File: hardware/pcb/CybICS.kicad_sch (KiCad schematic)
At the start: 75 parts, among them J1 Raspberry_Pi_2_3, J2 Conn_01x03_Pin, J3 Conn_01x05_Pin, SW1 SW_Push, SW2 SW_Push, SW3 SW_Push, U1 STM32G070RBTx

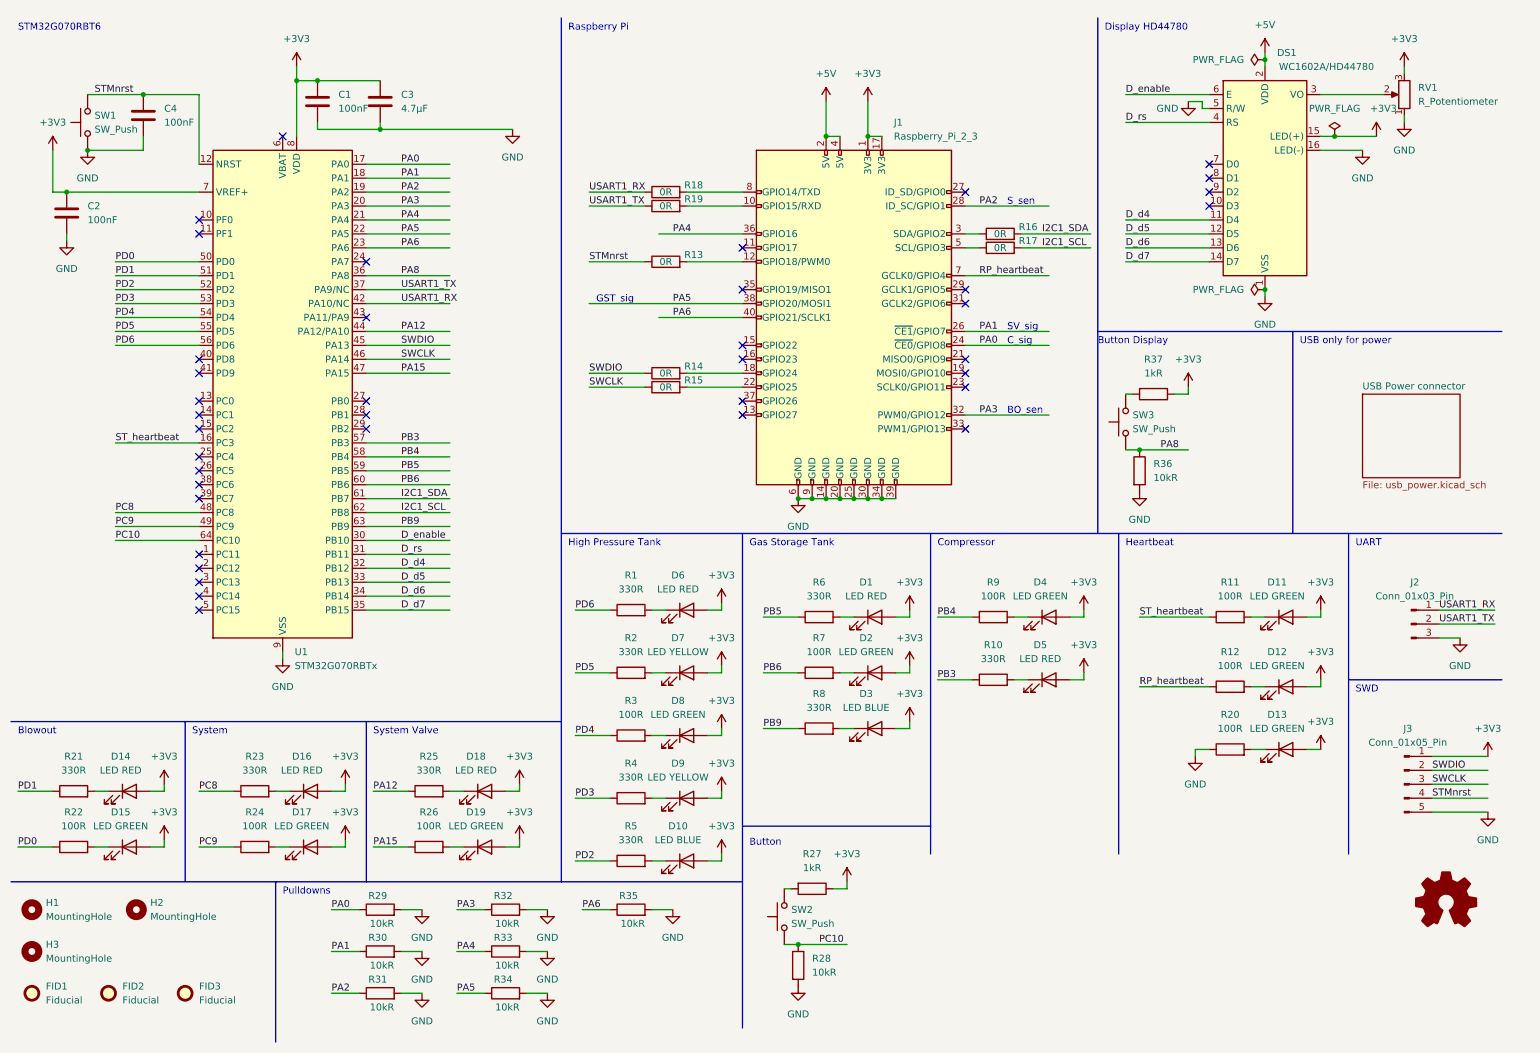
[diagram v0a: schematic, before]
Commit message: feat(hardware)!: hardware v1.1 upgrade, KiCad 10 and JLCPCB fixes (#240)
* fix(hardware): exclude fiducials from the JLCPCB position files

FID1-FID3 carried exclude_from_bom but not exclude_from_pos_files,
unlike the mounting holes and the OSHW logo, which set both. The
fiducials therefore reached the CPL while being absent from the BOM,
and JLCPCB rejected the assembly quote with "FID1,FID2,FID3
designators don't exist in the BOM file" (reported in #238). Fiducials
are alignment marks rather than parts, so the dialog was harmless, but
every person ordering this board had to decide that for themselves.

Verified with kicad-cli 8.0.9: pcb export pos --smd-only drops from 69
to 66 rows against the previous board, the three removed designators
are exactly FID1, FID2 and FID3, and ERC and DRC still report 0
violations and 0 unconnected items. Claude has no access to the
hardware, so the JLCPCB upload itself is unverified.

Refs #238

Co-Authored-By: Claude Opus 5 (1M context) <noreply@anthropic.com>
Claude-Session: https://claude.ai/code/session_011zbigHZaGiZii3etPu8DwT

* fix(hardware): correct the LED series resistors and the yellow LED part

R1/R2/R4/R6/R10/R21/R23/R25 are drawn as 330R but carried C52548, which
is 0805W8F330LT5E -- 330 mΩ, not 330 Ω. The L in that part code is
Uniroyal's milliohm marker, and both LCSC and JLCPCB's parts database
index it at 0.33 Ω. The six red, two yellow and two blue indicators
were therefore assembled with no effective current limiting: each one
settles at roughly its full rated current against the GPIO's own
impedance, and ten such pins take the STM32G070 past its 100 mA total
I/O budget. Corrected to C17630 (0805W8F3300T5E, 330 Ω), which is also
a basic-library part.

That correction alone would have regressed two colours, because the
0.33 Ω part was the only reason they lit at all:

  - D7/D9 are drawn as LED YELLOW but carried C434441, SZYY1206W -- a
    *white* LED with a yellow lens and Vf 3.1 V. Across a real 330 Ω
    fro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
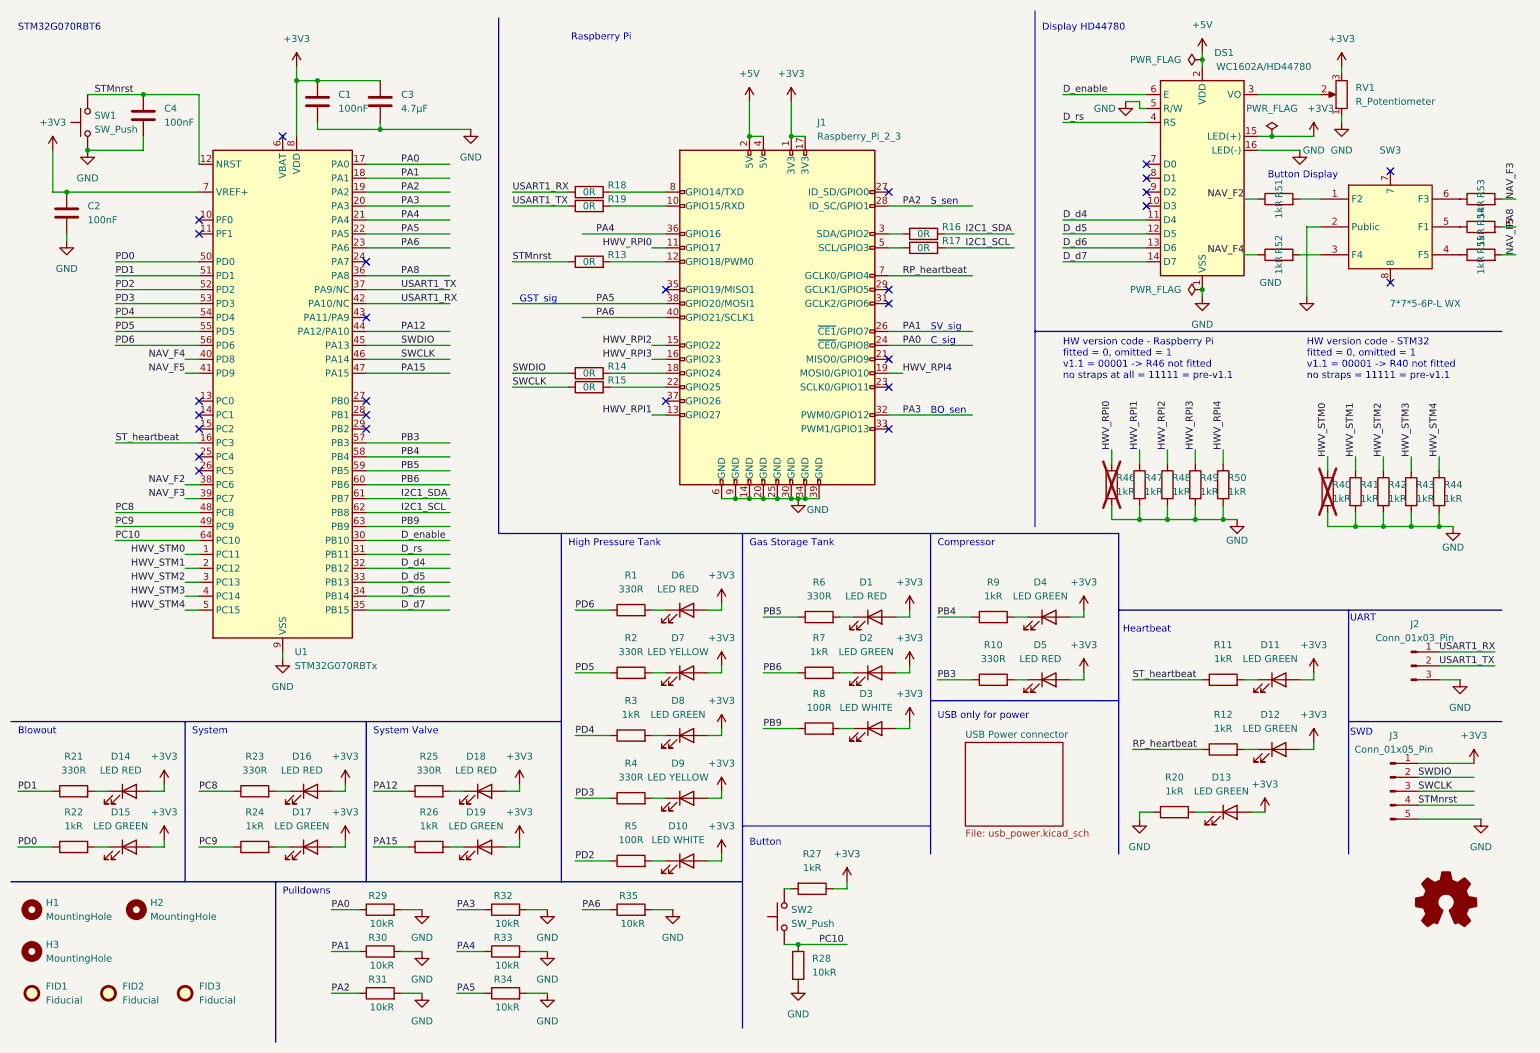
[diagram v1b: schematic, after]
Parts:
- removed R36: 10kR, Resistor_SMD:R_0805_2012Metric_Pad1.20x1.40mm_HandSolder, symbol Device:R
- removed R37: 1kR, Resistor_SMD:R_0805_2012Metric_Pad1.20x1.40mm_HandSolder, symbol Device:R
- removed SW3: SW_Push, Button_Switch_THT:SW_PUSH_6mm_H5mm, symbol Switch:SW_Push
- added R40, R41, R42, R43, R44, R46, R47, R48, R49, R50, R51, R52, R53, R54, R55: 1kR, Resistor_SMD:R_0805_2012Metric_Pad1.20x1.40mm_HandSolder, symbol Device:R
- added SW3: 7*7*5-6P-L WX, cybics:SW-SMD_8P-L7.0-W7.0-P1.40-LS7.4-TL, symbol cybics:SW_Nav_4Way_7x7
- C1, C2, C4: JLCPCB Part # C38141 -> C49678
- D1, D14, D16, D18, D5, D6: footprint LED_SMD:LED_1210_3225Metric_Pad1.42x2.65mm_HandSolder -> LED_SMD:LED_0805_2012Metric_Pad1.15x1.40mm_HandSolder; JLCPCB Part # C434438 -> C84256
- D10, D3: value LED BLUE -> LED WHITE; footprint LED_SMD:LED_1210_3225Metric_Pad1.42x2.65mm_HandSolder -> LED_SMD:LED_0805_2012Metric_Pad1.15x1.40mm_HandSolder; JLCPCB Part # C434440 -> C34499
- D11, D12, D13, D15, D17, D19, D2, D4, D8: footprint LED_SMD:LED_1210_3225Metric_Pad1.42x2.65mm_HandSolder -> LED_SMD:LED_0805_2012Metric_Pad1.15x1.40mm_HandSolder; JLCPCB Part # C434442 -> C2297
- D7, D9: footprint LED_SMD:LED_1210_3225Metric_Pad1.42x2.65mm_HandSolder -> LED_SMD:LED_0805_2012Metric_Pad1.15x1.40mm_HandSolder; JLCPCB Part # C434441 -> C2296
- J2: JLCPCB Part # C168677 -> C5445396
- R1, R10, R2, R21, R23, R25, R4, R6: JLCPCB Part # C52548 -> C17630
- R11, R12, R20, R22, R24, R26, R3, R7, R9: value 100R -> 1kR; JLCPCB Part # C17408 -> C17513
- R13, R14, R15, R16, R17, R18, R19: JLCPCB Part # C304192 -> C17477
- R5, R8: value 330R -> 100R; JLCPCB Part # C52548 -> C17408
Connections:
- net GND: now also R40.2, R41.2, R42.2, R43.2, R44.2, R46.2, R47.2, R48.2, R49.2, R50.2, SW3.2 (Public)
- net PA8: now also R54.2
- net HWV_RPI0: now reaches J1.11 (GPIO17)
- net HWV_RPI0: now also R46.1
- net HWV_RPI1: now reaches J1.13 (GPIO27)
- net HWV_RPI1: now also R47.1
- net HWV_RPI2: now reaches J1.15 (GPIO22)
- net HWV_RPI2: now also R48.1
- net HWV_RPI3: now reaches J1.16 (GPIO23)
- net HWV_RPI3: now also R49.1
- net HWV_RPI4: now reaches J1.19 (MOSI0/GPIO10)
- net HWV_RPI4: now also R50.1
- net HWV_STM0: now reaches U1.1 (PC11)
- net HWV_STM0: now also R40.1
- net HWV_STM1: now reaches U1.2 (PC12)
- net HWV_STM1: now also R41.1
- net HWV_STM2: now reaches U1.3 (PC13)
- net HWV_STM2: now also R42.1
- net NAV_F2: now reaches U1.38 (PC6)
- net NAV_F2: now also R51.1
- net NAV_F3: now reaches U1.39 (PC7)
- net NAV_F3: now also R53.2
- net HWV_STM3: now reaches U1.4 (PC14)
- net HWV_STM3: now also R43.1
- net NAV_F4: now reaches U1.40 (PD8)
- net NAV_F4: now also R52.1
- net NAV_F5: now reaches U1.41 (PD9)
- net NAV_F5: now also R55.2
- net HWV_STM4: now reaches U1.5 (PC15)
- net HWV_STM4: now also R44.1
- new net: R55.1, SW3.4 (F5)
- new net: R53.1, SW3.6 (F3)
- new net: R52.2, SW3.3 (F4)
- new net: R51.2, SW3.1 (F2)
- new net: R54.1, SW3.5 (F1)
- no-connect marks 39 -> 27
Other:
- note added: "HW version code - Raspberry Pi fitted = 0, omitted = 1 v1.1 = 00001 -> R46 not fitted no straps at all = 11111 = pre-v1.1"
- note added: "HW version code - STM32 fitted = 0, omitted = 1 v1.1 = 00001 -> R40 not fitted no straps = 11111 = pre-v1.1"
- moved on the sheet: D11, D12, D13, DS1, J1, J2, J3, R11, R12, R13, R14, R15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

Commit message: fix: balance the LED brightness on v1.1 boards (#274)
* fix(hardware): fit 20k to the three status LEDs on v1.1

The three greens on the left edge -- D11 (STM32 heartbeat), D12
(Raspberry Pi heartbeat) and D13 (power) -- sit on 1k, and v1.1's green,
C2297, is efficient enough that they glare at that current. D13 is tied
straight to 3V3 and cannot be dimmed from either controller at all. On a
board reworked to 20k for R11, R12 and R20 the brightness was judged
acceptable by eye, so the v1.1 BOM now fits that value: UNI-ROYAL
0805W8F2002T5E, JLCPCB Basic part C4328, the same 0805 family as the
C17513 1k it replaces.

Only the Value and JLCPCB Part # fields of R11, R12 and R20 change, in
the schematic and on the board; footprints, nets and layout are
untouched.

Verified with setsoft/kicad_auto:ki10 (KiCad 10): ERC with errors as
failures exits 0, DRC with --schematic-parity reports 0 violations and 0
unconnected pads, and the exported BOM groups "R11,R12,R20 / 20kR /
C4328". The generated docs under hardware/pcb/docs are left to
kibotVerify.yml.

Co-Authored-By: Claude Opus 5.5 <noreply@anthropic.com>

* fix(stm32): dim the process LEDs per board revision

The output thread has always run every LED except the greens at about
one fifteenth duty and left the greens fully on. That suited v1.0, whose
green part was much dimmer than its red, yellow and blue. v1.1 moved all
LEDs to JLCPCB Basic parts, and its green (C2297) is an order of
magnitude more efficient: on a v1.1 board the greens glare while red,
yellow and white look faint.

Brightness is now a table per board revision and per colour, chosen at
start-up from the version straps. The v1.0 table reproduces the old
behaviour exactly; v1.1 and unknown newer boards get green 10 %, red
40 %, yellow 50 % and white 15 %, the shares tuned by eye on a v1.1 board
on the earlier fix/green-led-brightness branch. The PWM runs at 100 Hz
and wakes once per colour per period, using the 10 kHz kernel tick for
1 % resolution.

The t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
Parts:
- R11, R12, R20: value 1kR -> 20kR; JLCPCB Part # C17513 -> C4328
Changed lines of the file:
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@@
 			)
 		)
-		(property "Value" "1kR"
+		(property "Value" "20kR"
 			(at 233.68 129.54 90)
 			(show_name no)
@@
 			)
 		)
-		(property "JLCPCB Part #" "C17513"
+		(property "JLCPCB Part #" "C4328"
 			(at 233.68 133.35 90)
 			(hide yes)
@@
 			)
 		)
-		(property "Value" "1kR"
+		(property "Value" "20kR"
 			(at 224.79 153.67 90)
 			(show_name no)
@@
 			)
 		)
-		(property "JLCPCB Part #" "C17513"
+		(property "JLCPCB Part #" "C4328"
 			(at 224.79 157.48 90)
 			(hide yes)
@@
 			)
 		)
-		(property "Value" "1kR"
+		(property "Value" "20kR"
 			(at 233.68 142.24 90)
 			(show_name no)
@@
 			)
 		)
-		(property "JLCPCB Part #" "C17513"
+		(property "JLCPCB Part #" "C4328"
 			(at 233.68 146.05 90)
 			(hide yes)
